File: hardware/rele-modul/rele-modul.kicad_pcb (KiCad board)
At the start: 4 copper layers, 68 x 86.5 mm, 86 parts, among them J1 DEBUG, J100 24V IN, J101 RELÉ 1, J102 RELÉ 2, J103 RELÉ 3, J104 RELÉ 4, J105 SCT-013, J2 BUS_IN, J3 BUS_OUT, J4 BŐVÍTŐ, K1 RTD14024, K2 RTD14024, K3 RTD14024, K4 RTD14024, Q100 IRFR120N, U101 ULN2803ADWR, U2 SN65HVD230D, U3 ESD2CAN24-Q1, U5 AP2112K-3.3TRG1, U6 STM32L433RCT3, Y1 8MHz

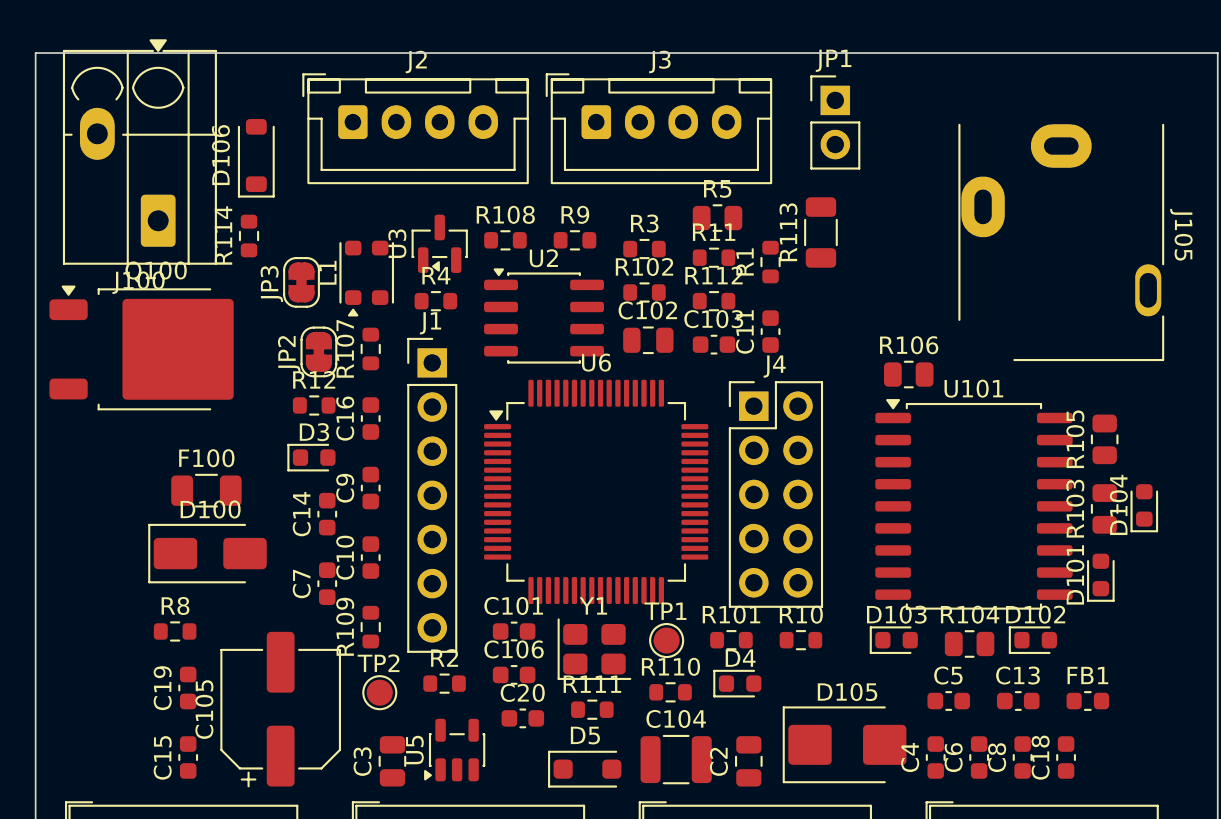
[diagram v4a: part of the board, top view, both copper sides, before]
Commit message: Hardver: legolcsóbb beszerzés LCSC-ről (D85), megszűnt FET-ek pótlása, LCSC-kosárlista
- gen/lcsc.py: LCSC-árak a JLC alkatrészkeresőjéből; gen/beszerzes.py soronként a legolcsóbb forrás (Hestore / LCSC, ÁFA-val)
- bom/lcsc-kosar.csv: 99 tétel (~15 eFt), az LCSC BOM Tooljába feltölthető; házak később, ST-Link/Nucleo kézben
- Q202–Q207 NTD5C648NL → NCE6080K, Q201 NTMFS5C604NL → NCEP6090AGU (nem kaphatók), F201 → NANO² 15 A,
  D211–D216 SS56B, J1/J100 DG128, L1/L3 LCSC-s 0630-as tekercs, kis ESR-ű kvarcok
- bekötés változatlan (netlista 0 / 0), ellenorzes.py: 0 hiba

Co-Authored-By: Claude Opus 5.5 <noreply@anthropic.com>
Claude-Session: https://claude.ai/code/session_01KVtZMUPbtveTXy9VyJshyt
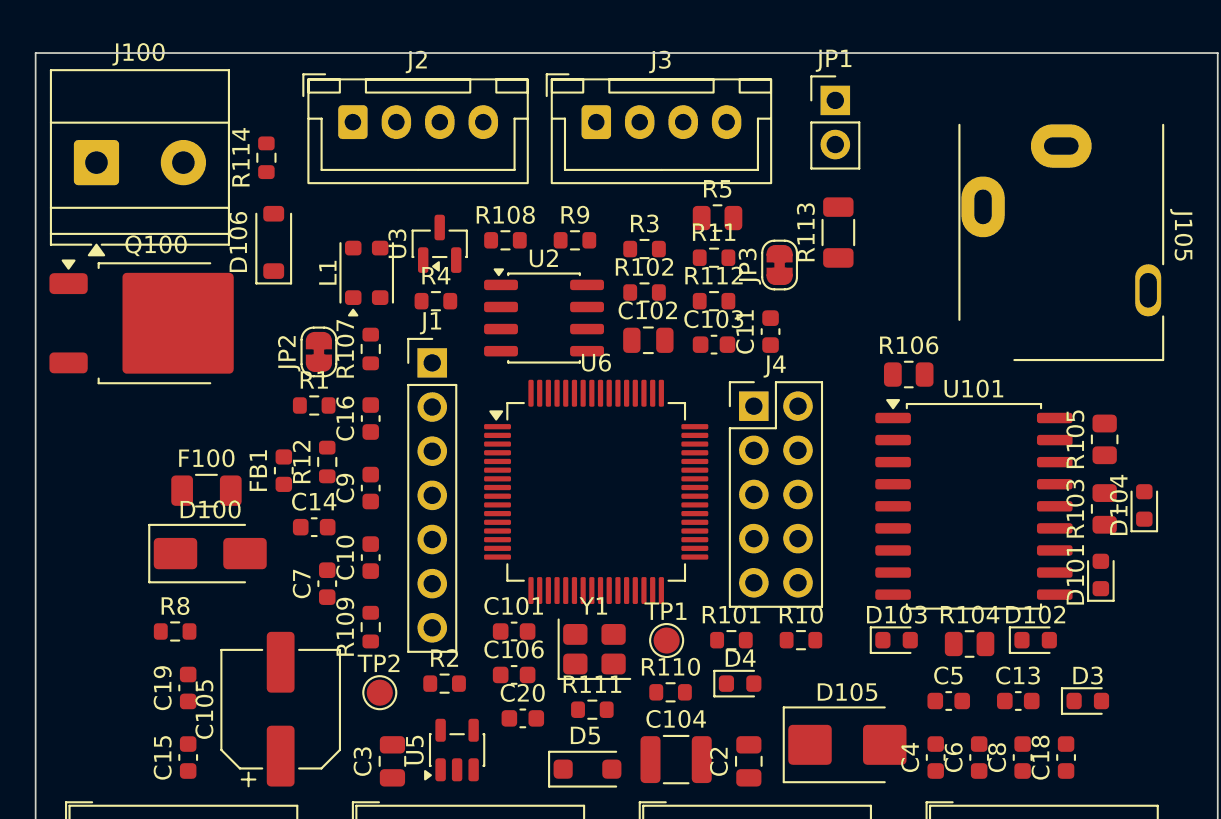
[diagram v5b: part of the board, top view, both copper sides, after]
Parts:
- J100: footprint TerminalBlock_Degson:TerminalBlock_Degson_DG250-3.5-02P_1x02_P3.50mm_45Degree -> TerminalBlock_Phoenix:TerminalBlock_Phoenix_MKDS-1,5-2_1x02_P5.00mm_Horizontal
- moved FB1 48.1 mm to (114.3, 124.0), turned to 90 degrees
- moved D3 46.7 mm to (160.5, 137.3)
- moved JP3 27.5 mm to (142.8, 112.2)
- moved R1 27.5 mm to (116.0, 120.3), turned to 0 degrees
- moved D106 5.10 mm to (113.7, 110.9)
- moved J100 4.88 mm to (103.5, 106.3), turned to 0 degrees
- moved R114 4.61 mm to (113.3, 106.0)
- moved R12 3.34 mm to (116.8, 123.5), turned to 90 degrees
- moved Q100 1.50 mm to (106.9, 115.5)
- moved C14 1.06 mm to (116.0, 127.3), turned to 0 degrees
- moved R113 1.00 mm to (146.2, 110.3)

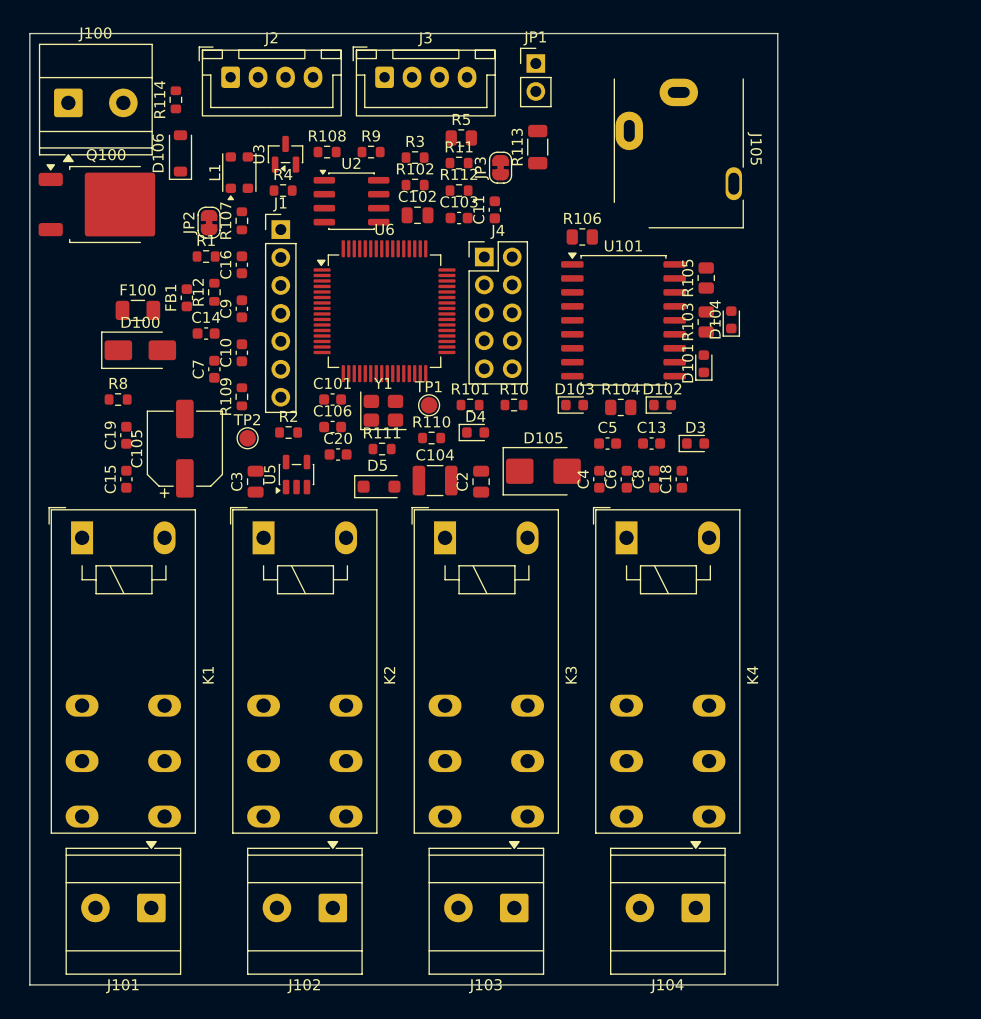
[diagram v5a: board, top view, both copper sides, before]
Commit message: Hardver: layout-előkészítés (D86) – JLC-szabályok és via-méretek, modulmag-blokk, a modulok elrendezése
- laponként .kicad_dru: JLC 4 réteg / 1 oz; via 0,3/0,45 (jel), 0,4/0,7 (táp), 0,6/1,0 mm (15 A); 230 V ↔ SELV 8 mm
- modulmag-blokk mindhárom modulon azonos relatív elrendezéssel (átvihető layout), 0,25 mm-es rács
- a sorkapcsok a Gainta D4MG fedélfurataira igazítva (5,08 mm), a kötött helyű alkatrészek zárolva
- LED-modul: LED-sor, meghajtók, FET-sor; relé: betáp és LED-sor; bemeneti: csatornánkénti oszlopok, ESD-sor
- lábhoz rendelés: hidegítők a tápjukhoz, gate-ellenállások a gate-hez; a vezérlő elrendezése még hátra (U4)
- docs/d4mg.pdf: a ház rajza; ellenorzes.py: 0 hiba

Co-Authored-By: Claude Opus 5.5 <noreply@anthropic.com>
Claude-Session: https://claude.ai/code/session_01KVtZMUPbtveTXy9VyJshyt
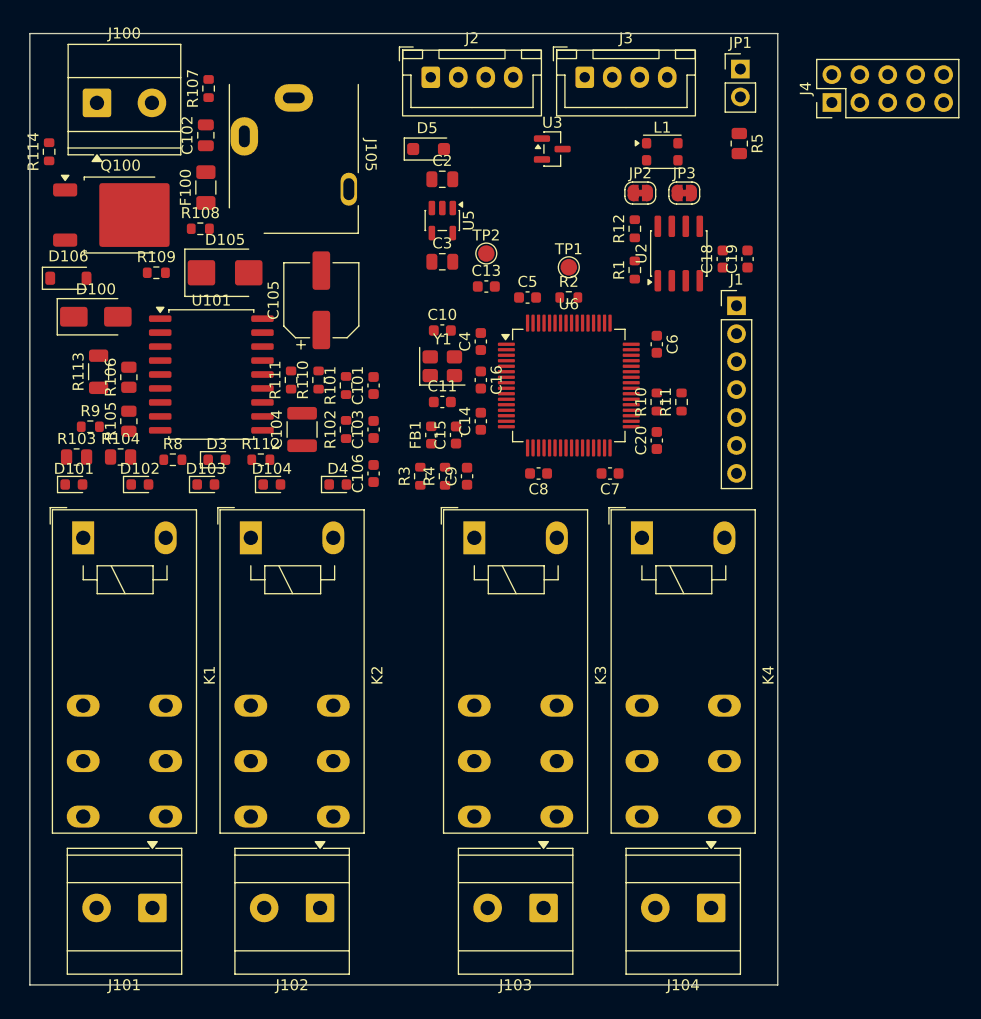
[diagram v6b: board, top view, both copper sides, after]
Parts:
- moved C19 58.7 mm to (165.2, 120.5)
- moved R103 58.5 mm to (104.2, 138.5), turned to 0 degrees
- moved D101 58.3 mm to (104.0, 141.0), turned to 0 degrees
- moved R105 54.1 mm to (109.0, 135.2)
- moved D102 48.1 mm to (110.0, 141.0)
- moved R104 45.7 mm to (108.2, 138.5)
- moved R113 44.8 mm to (106.2, 130.8)
- moved D104 44.4 mm to (122.0, 141.0), turned to 0 degrees
- moved D3 43.5 mm to (117.0, 138.8)
- moved R106 43.2 mm to (109.0, 131.2), turned to 90 degrees
- moved J1 42.0 mm to (164.2, 124.8)
- moved JP2 39.3 mm to (155.5, 114.5), turned to 0 degrees
- moved R1 39.0 mm to (155.0, 121.5), turned to 90 degrees
- moved R12 38.7 mm to (155.0, 117.8)
- moved L1 38.5 mm to (157.5, 110.8), turned to 0 degrees
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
